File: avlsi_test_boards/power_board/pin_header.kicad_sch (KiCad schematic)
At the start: 1 part

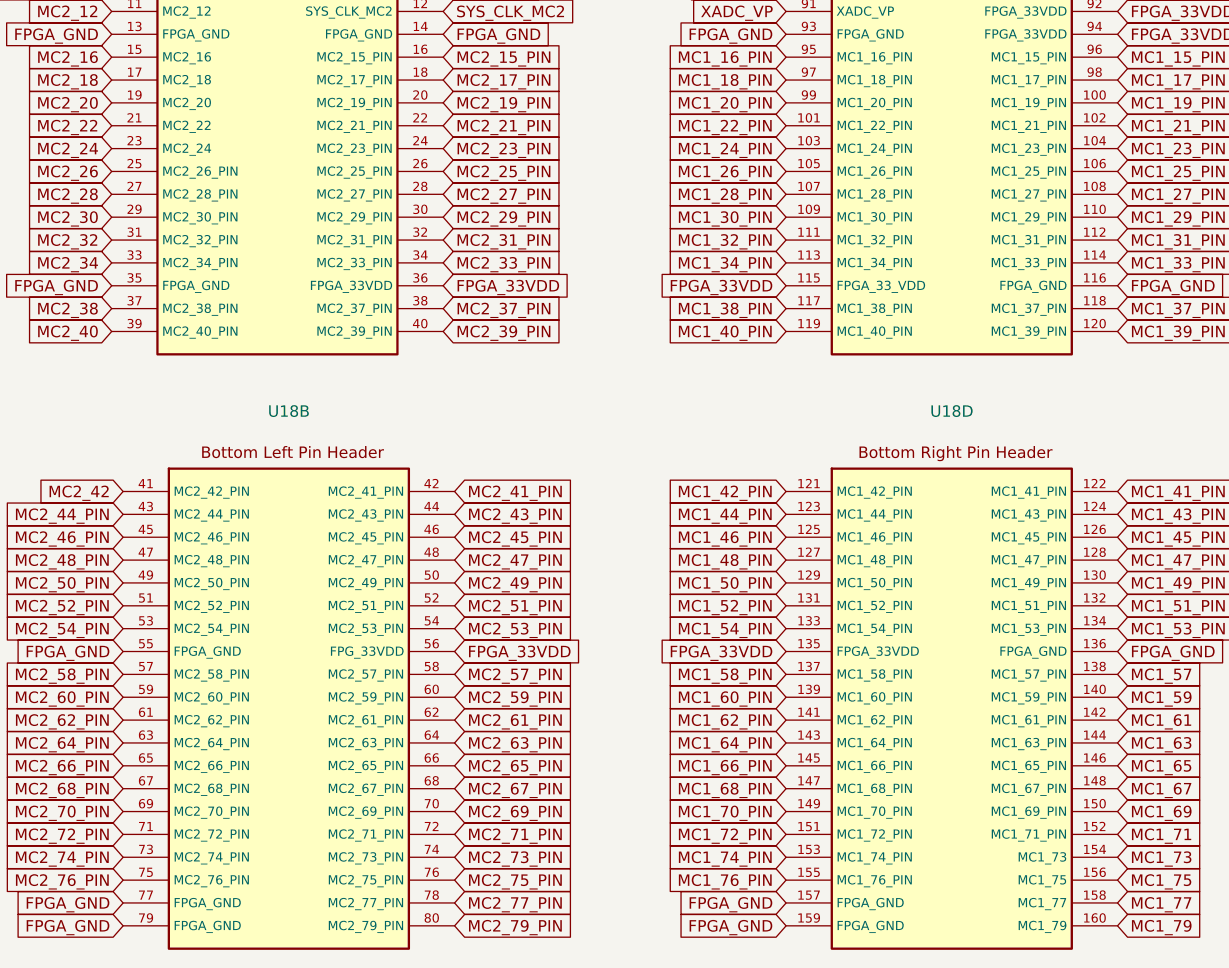
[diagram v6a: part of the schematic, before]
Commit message: Add updated symbol
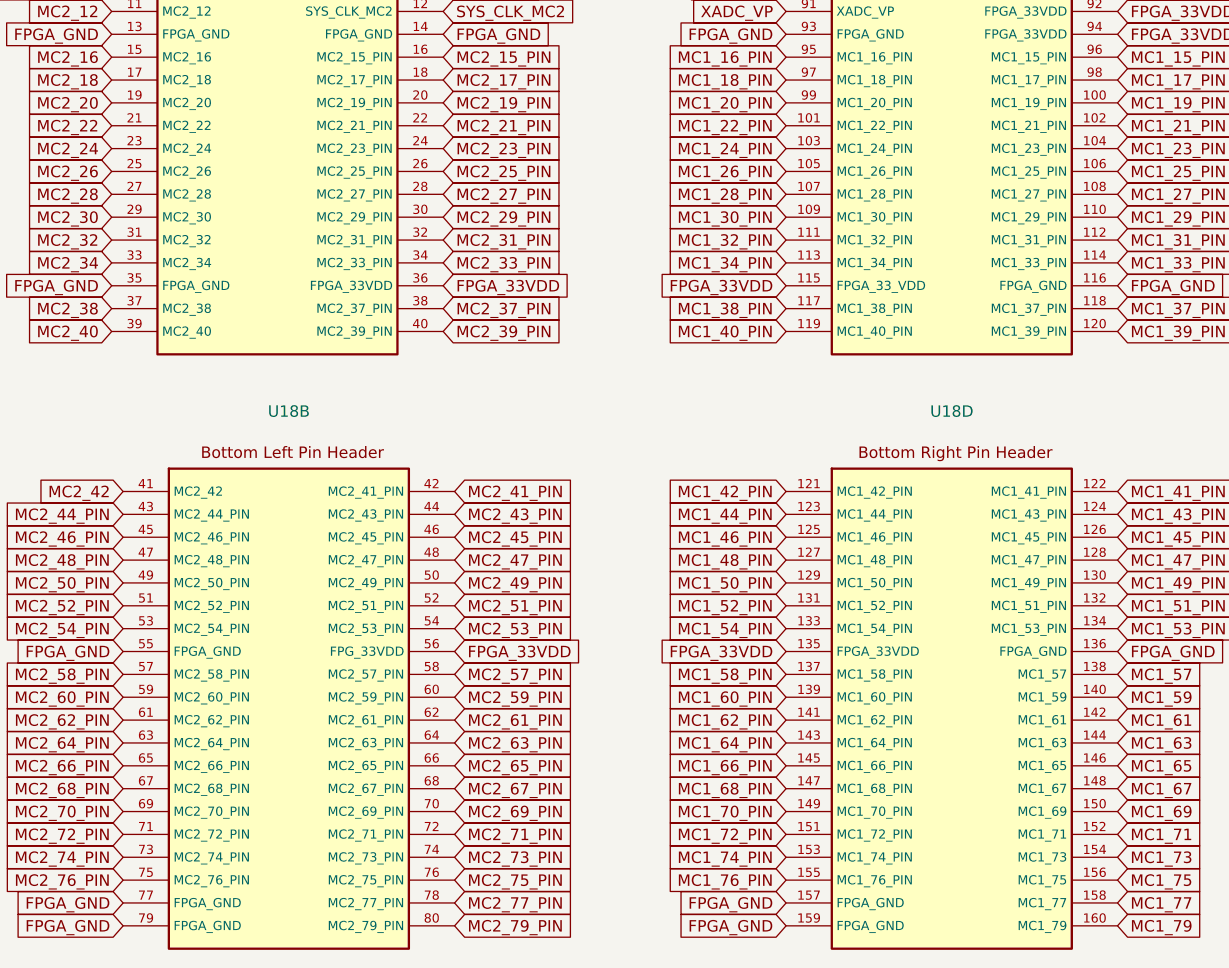
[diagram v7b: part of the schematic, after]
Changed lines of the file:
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@@
 	)
 	(symbol
+		(lib_name "avlsi_power_board_opal_kelly_2")
 		(lib_id "avlsi_preferred_parts:avlsi_power_board_opal_kelly")
 		(at 48.26 46.99 0)
@@
 	)
 	(symbol
+		(lib_name "avlsi_power_board_opal_kelly_3")
 		(lib_id "avlsi_preferred_parts:avlsi_power_board_opal_kelly")
 		(at 49.53 113.03 0)
@@
 	)
 	(symbol
+		(lib_name "avlsi_power_board_opal_kelly_1")
 		(lib_id "avlsi_preferred_parts:avlsi_power_board_opal_kelly")
 		(at 123.19 113.03 0)
@@
 	)
 	(symbol
+		(lib_name "avlsi_power_board_opal_kelly_4")
 		(lib_id "avlsi_preferred_parts:avlsi_power_board_opal_kelly")
 		(at 123.19 46.99 0)

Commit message: Update schematic
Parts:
- removed U18: ~, avlsi_preferred_parts:avlsi_power_board_opal_kelly, symbol avlsi_preferred_parts:avlsi_power_board_opal_kelly
- added J5, J6: Conn_01x02_Pin, Connector_PinHeader_2.54mm:PinHeader_1x02_P2.54mm_Horizontal, symbol Connector:Conn_01x02_Pin
- added U18: ~, avlsi_preferred_parts:power_board, symbol avlsi_preferred_parts:Power_Board
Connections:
- net AVIN5: now also U18.173 (AVIN5)
- net DGND: now also J6.2 (Pin_2), U18.176 (DGND), U18.180 (DGND), U18.182 (DGND), U18.184 (DGND), U18.186 (DGND), U18.188 (DGND), U18.190 (DGND), U18.191 (DGND), U18.192 (DGND), U18.193 (DGND), U18.194 (DGND)
- net DVIN5: now also U18.189 (DVIN5)
- net FPGA_10VDD: now also U18.83 (VCCBATT), U18.85 (FPGA_TCK)
- net FPGA_18VDD: now also U18.88 (FPGA_TDO)
- net FPGA_33VDD: now also U18.01 (VCDIN), U18.03 (VDCIN), U18.05 (VDCIN), U18.115 (VCCO_MC2), U18.135 (VCCO_MC2), U18.36 (VCCO_MC1), U18.56 (VCCO_MC1), U18.90 (MC2_10), U18.92 (MC2_12), U18.94 (DGND)
- net FPGA_GND: now also U18.02 (DGND), U18.116 (DGND), U18.13 (33VDD), U18.136 (DGND), U18.14 (DGND), U18.157 (MC2_77), U18.159 (MC2_79), U18.35 (DGND), U18.55 (DGND), U18.77 (MC1_77), U18.79 (MC1_79), U18.81 (DGND), U18.93 (DGND)
- net FPGA_TCK: now also U18.06 (10VDD)
- net FPGA_TDI: now also U18.10 (XADC_VN)
- net FPGA_TDO: now also U18.07 (18VDD)
- net FPGA_TMS: now also U18.08 (SYS_CLK_MC1)
- net FPGA_VCDIN: now also U18.82 (33VDD), U18.84 (33VDD), U18.86 (33VDD)
- net MC1_15_PIN: now also U18.96 (MC2_16)
- net MC1_16_PIN: now also U18.95 (MC2_15)
- net MC1_17_PIN: now also U18.98 (MC2_18)
- net MC1_18_PIN: now also U18.97 (MC2_17)
- net MC1_19_PIN: now also U18.100 (MC2_20)
- net MC1_20_PIN: now also U18.99 (MC2_19)
- net MC1_21_PIN: now also U18.102 (MC2_22)
- net MC1_22_PIN: now also U18.101 (MC2_21)
- net MC1_23_PIN: now also U18.104 (MC2_24)
- net MC1_24_PIN: now also U18.103 (MC2_23)
- net MC1_25_PIN: now also U18.106 (MC2_26)
- net MC1_26_PIN: now also U18.105 (MC2_25)
- net MC1_27_PIN: now also U18.108 (MC2_28)
- net MC1_28_PIN: now also U18.107 (MC2_27)
- net MC1_29_PIN: now also U18.110 (MC2_30)
- net MC1_30_PIN: now also U18.109 (MC2_29)
- net MC1_31_PIN: now also U18.112 (MC2_32)
- net MC1_32_PIN: now also U18.111 (MC2_31)
- net MC1_33_PIN: now also U18.114 (MC2_34)
- net MC1_34_PIN: now also U18.113 (MC2_33)
- net MC1_37_PIN: now also U18.118 (MC2_38)
- net MC1_38_PIN: now also U18.117 (MC2_37)
- net MC1_39_PIN: now also U18.120 (MC2_40)
- net MC1_40_PIN: now also U18.119 (MC2_39)
- net MC1_41_PIN: now also U18.122 (MC2_42)
- net MC1_42_PIN: now also U18.121 (MC2_41)
- net MC1_43_PIN: now also U18.124 (MC2_44)
- net MC1_44_PIN: now also U18.123 (MC2_43)
- net MC1_45_PIN: now also U18.126 (MC2_46)
- net MC1_46_PIN: now also U18.125 (MC2_45)
- net MC1_47_PIN: now also U18.128 (MC2_48)
- net MC1_48_PIN: now also U18.127 (MC2_47)
- net MC1_49_PIN: now also U18.130 (MC2_50)
- net MC1_50_PIN: now also U18.129 (MC2_49)
- net MC1_51_PIN: now also U18.132 (MC2_52)
- net MC1_52_PIN: now also U18.131 (MC2_51)
- net MC1_53_PIN: now also U18.134 (MC2_54)
- net MC1_54_PIN: now also U18.133 (MC2_53)
- net MC1_57: now also U18.138 (MC2_58)
- net MC1_58_PIN: now also U18.137 (MC2_57)
- net MC1_59: now also U18.140 (MC2_60)
- net MC1_60_PIN: now also U18.139 (MC2_59)
- net MC1_61: now also U18.142 (MC2_62)
- net MC1_62_PIN: now also U18.141 (MC2_61)
- net MC1_63: now also U18.144 (MC2_64)
- net MC1_64_PIN: now also U18.143 (MC2_63)
- net MC1_65: now also U18.146 (MC2_66)
- net MC1_66_PIN: now also U18.145 (MC2_65)
- net MC1_67: now also U18.148 (MC2_68)
- net MC1_68_PIN: now also U18.147 (MC2_67)
- net MC1_69: now also U18.150 (MC2_70)
- net MC1_70_PIN: now also U18.149 (MC2_69)
- net MC1_71: now also U18.152 (MC2_72)
- net MC1_72_PIN: now also U18.151 (MC2_71)
- net MC1_73: now also U18.154 (MC2_74)
- net MC1_74_PIN: now also U18.153 (MC2_73)
- net MC1_75: now also U18.156 (MC2_76)
- net MC1_76_PIN: now also U18.155 (MC2_75)
- net MC1_77: now also U18.158 (DGND)
- net MC1_79: now also U18.160 (DGND)
- net MC2_10_PIN: now also U18.09 (33VDD)
- net MC2_12: now also U18.11 (33VDD)
- net MC2_15_PIN: now also U18.16 (MC1_16)
- net MC2_16: now also U18.15 (MC1_15)
- net MC2_17_PIN: now also U18.18 (MC1_18)
- net MC2_18: now also U18.17 (MC1_17)
- net MC2_19_PIN: now also U18.20 (MC1_20)
- net MC2_20: now also U18.19 (MC1_19)
- net MC2_21_PIN: now also U18.22 (MC1_22)
- net MC2_22: now also U18.21 (MC1_21)
- net MC2_23_PIN: now also U18.24 (MC1_24)
- net MC2_24: now also U18.23 (MC1_23)
- net MC2_25_PIN: now also U18.26 (MC1_26)
- net MC2_26: now also U18.25 (MC1_25)
- net MC2_27_PIN: now also U18.28 (MC1_28)
- net MC2_28: now also U18.27 (MC1_27)
- net MC2_29_PIN: now also U18.30 (MC1_30)
- net MC2_30: now also U18.29 (MC1_29)
- net MC2_31_PIN: now also U18.32 (MC1_32)
- net MC2_32: now also U18.31 (MC1_31)
- net MC2_33_PIN: now also U18.34 (MC1_34)
- net MC2_34: now also U18.33 (MC1_33)
- net MC2_37_PIN: now also U18.38 (MC1_38)
- net MC2_38: now also U18.37 (MC1_37)
- net MC2_39_PIN: now also U18.40 (MC1_40)
- net MC2_40: now also U18.39 (MC1_39)
- net MC2_41_PIN: now also U18.42 (MC1_42)
- net MC2_42: now also U18.41 (MC1_41)
- net MC2_43_PIN: now also U18.44 (MC1_44)
- net MC2_44_PIN: now also U18.43 (MC1_43)
- net MC2_45_PIN: now also U18.46 (MC1_46)
- net MC2_46_PIN: now also U18.45 (MC1_45)
- net MC2_47_PIN: now also U18.48 (MC1_48)
- net MC2_48_PIN: now also U18.47 (MC1_47)
- net MC2_49_PIN: now also U18.50 (MC1_50)
- net MC2_50_PIN: now also U18.49 (MC1_49)
- net MC2_51_PIN: now also U18.52 (MC1_52)
- net MC2_52_PIN: now also U18.51 (MC1_51)
- net MC2_53_PIN: now also U18.54 (MC1_54)
- net MC2_54_PIN: now also U18.53 (MC1_53)
- net MC2_57_PIN: now also U18.58 (MC1_58)
- net MC2_58_PIN: now also U18.57 (MC1_57)
- net MC2_59_PIN: now also U18.60 (MC1_60)
- net MC2_60_PIN: now also U18.59 (MC1_59)
- net MC2_61_PIN: now also U18.62 (MC1_62)
- net MC2_62_PIN: now also U18.61 (MC1_61)
- net MC2_63_PIN: now also U18.64 (MC1_64)
- net MC2_64_PIN: now also U18.63 (MC1_63)
- net MC2_65_PIN: now also U18.66 (MC1_66)
- net MC2_66_PIN: now also U18.65 (MC1_65)
- net MC2_67_PIN: now also U18.68 (MC1_68)
- net MC2_68_PIN: now also U18.67 (MC1_67)
- net MC2_69_PIN: now also U18.70 (MC1_70)
- net MC2_70_PIN: now also U18.69 (MC1_69)
- net MC2_71_PIN: now also U18.72 (MC1_72)
- net MC2_72_PIN: now also U18.71 (MC1_71)
- net MC2_73_PIN: now also U18.74 (MC1_74)
- net MC2_74_PIN: now also U18.73 (MC1_73)
- net MC2_75_PIN: now also U18.76 (MC1_76)
- net MC2_76_PIN: now also U18.75 (MC1_75)
- net MC2_77_PIN: now also U18.78 (DGND)
- net MC2_79_PIN: now also U18.80 (DGND)
- net SYS_CLK_MC1: now also U18.87 (FPGA_TMS)
- net SYS_CLK_MC2: now also U18.12 (XADC_VP)
- net VCCA09: now also U18.163 (VCCA09)
- net VCCA12: now also U18.165 (VCCA12)
- net VCCA18: now also U18.167 (VCCA18)
- net VCCA25: now also U18.169 (VCCA25)
- net VCCA33: now also U18.171 (VCCA33)
- net VCCACUSTOM: now also J5.1 (Pin_1), U18.161 (VCCACUSTOM)
- net VCCBATT: now also U18.04 (10VDD)
- net VCCD09: now also U18.179 (VCCD09)
- net VCCD12: now also U18.181 (VCCD12)
- net VCCD18: now also U18.183 (VCCD18)
- net VCCD25: now also U18.185 (VCCD25)
- net VCCD33: now also U18.187 (VCCD33)
- net VDCustom: now also J6.1 (Pin_1), U18.175 (VDCUSTOM)
- net XADC_VN: now also U18.89 (FPGA_TDI)
- net XADC_VP: now also U18.91 (SYS_CLK_MC2)
- new net AGND: J5.2 (Pin_2), U18.162 (AGND), U18.164 (AGND), U18.166 (AGND), U18.168 (AGND), U18.170 (AGND), U18.172 (AGND), U18.174 (AGND)
